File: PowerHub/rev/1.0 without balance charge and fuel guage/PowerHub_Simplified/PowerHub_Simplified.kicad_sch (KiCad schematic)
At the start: 28 parts, among them J1 HUB_CONN_1_W_VBUS, J2 HUB_CONN_2_W_VBUS, J3 HUB_CONN_3, J4 HUB_CONN_4, J5 BATTERY-, J6 BATTERY+, J7 Charger, Q1 BC817, SW1 SW_SPST, U1 TPS565208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

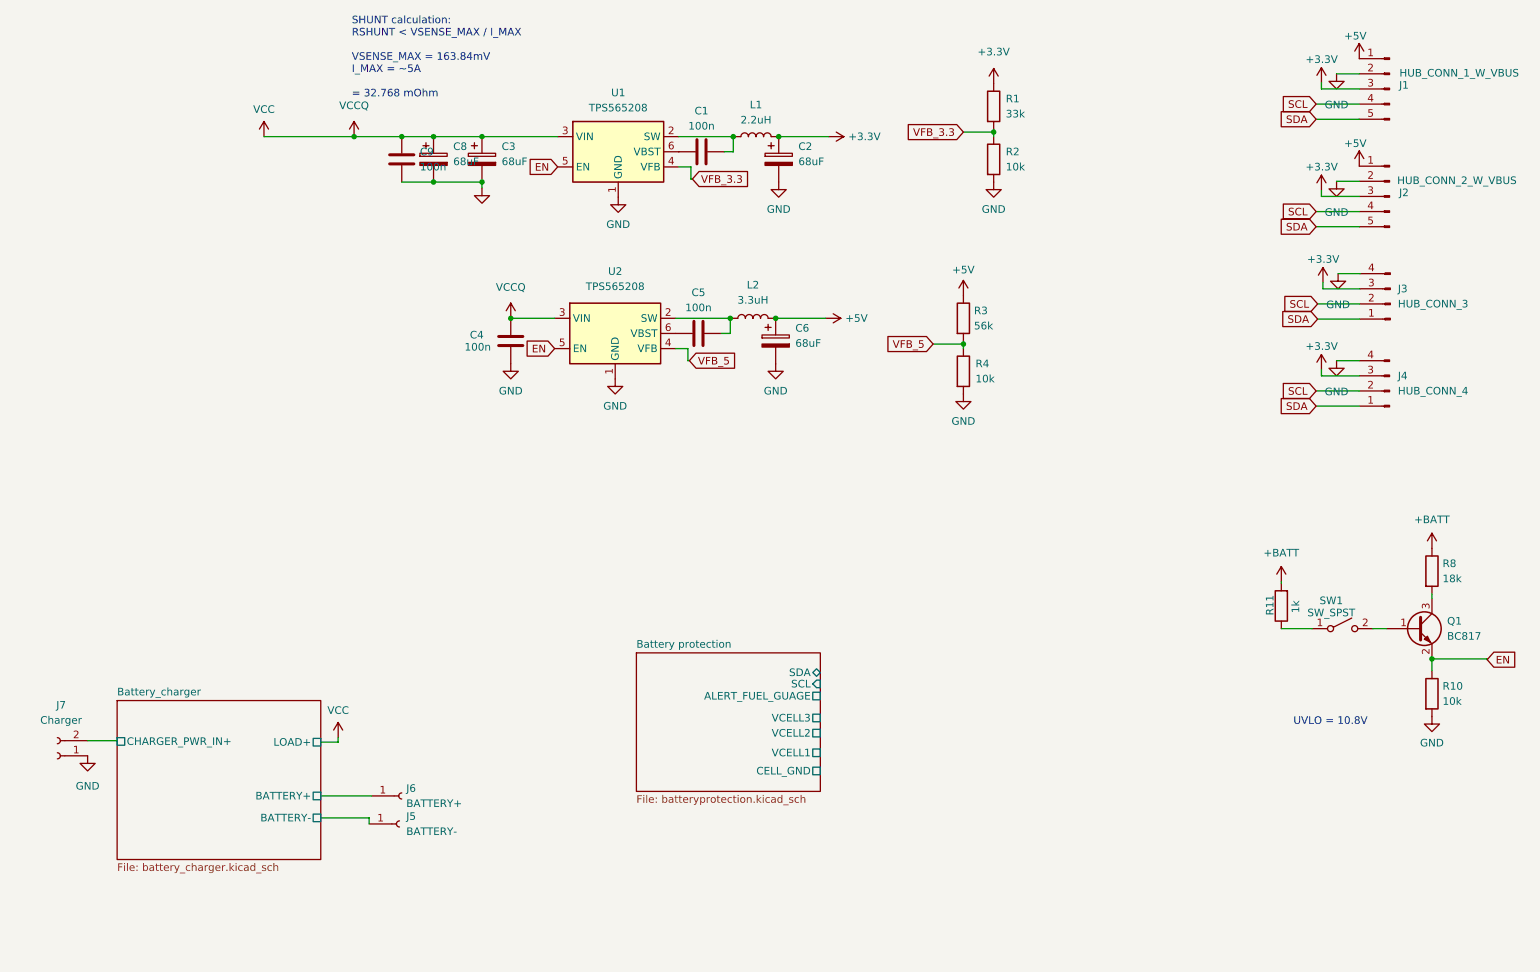
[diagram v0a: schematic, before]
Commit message: -add new version with charger circuit
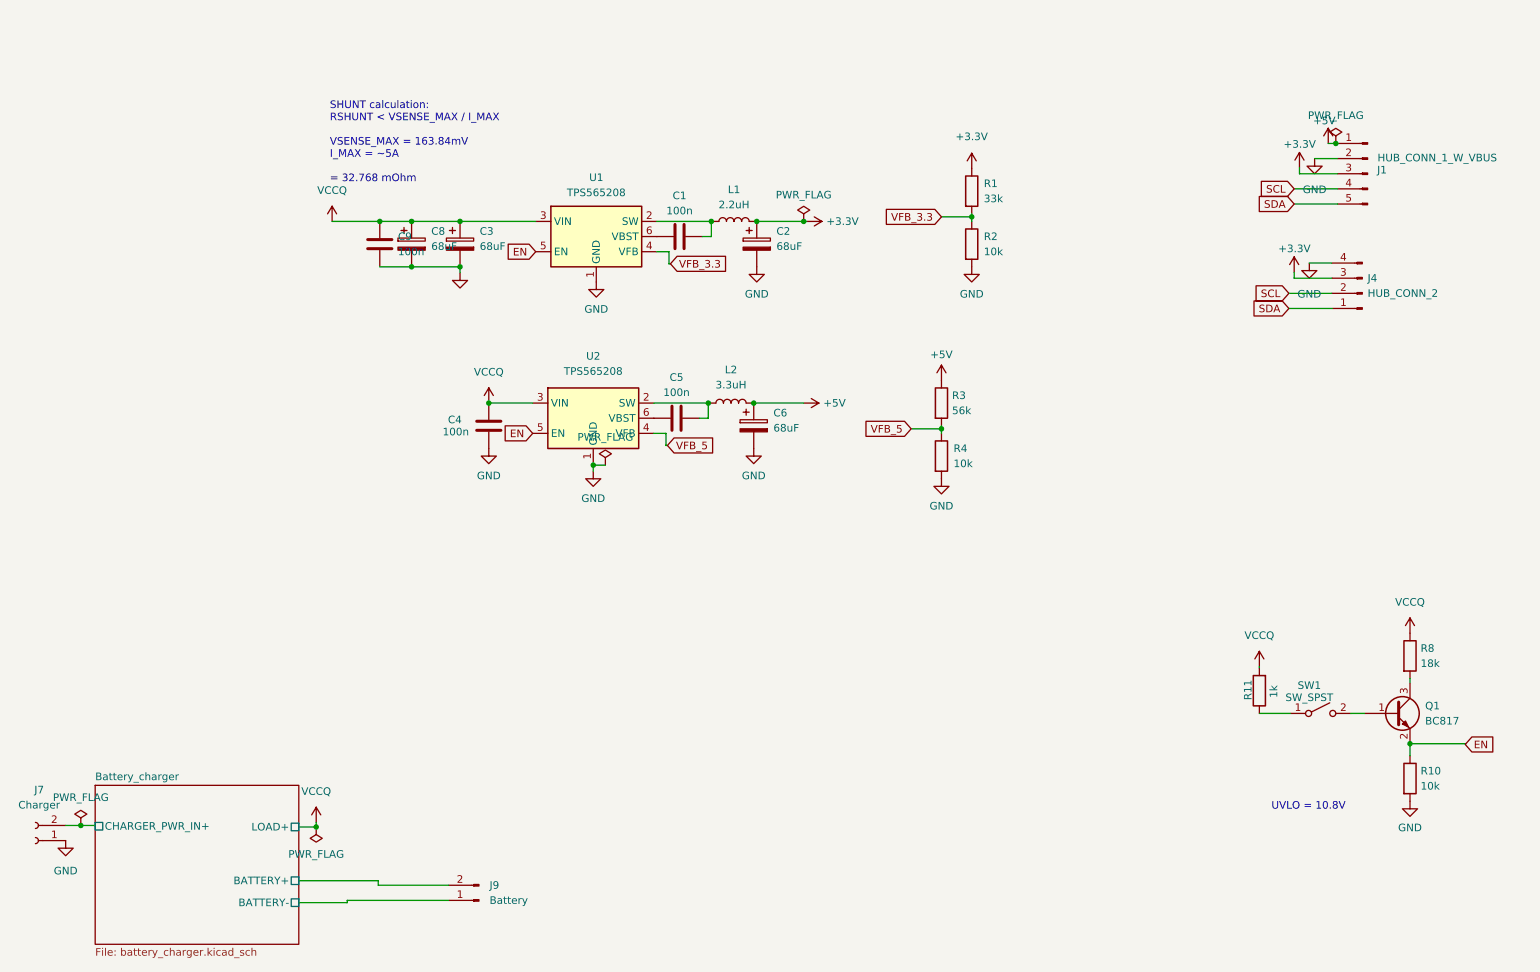
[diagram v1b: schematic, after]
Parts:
- removed J2: HUB_CONN_2_W_VBUS, symbol Connector:Conn_01x05_Pin
- removed J3: HUB_CONN_3, symbol Connector:Conn_01x04_Pin
- removed J5: BATTERY-, symbol Connector:Conn_01x01_Socket
- removed J6: BATTERY+, symbol Connector:Conn_01x01_Socket
- added J9: Battery, PowerHub_libs:1814773, symbol Connector:Conn_01x02_Pin
- C1, C4, C5, C9: footprint (none) -> Capacitor_SMD:C_0603_1608Metric_Pad1.08x0.95mm_HandSolder
- C2, C3, C6, C8: footprint (none) -> Capacitor_SMD:C_Elec_6.3x7.7
- J1: footprint (none) -> PowerHub_libs:1814809
- J4: value HUB_CONN_4 -> HUB_CONN_2; footprint (none) -> PowerHub_libs:SHDRRA4W60P0X250_1X4_1170X750X510P
- J7: footprint (none) -> PowerHub_libs:1814773
- L1, L2: footprint (none) -> Inductor_SMD:L_Abracon_ASPI-0630LR
- R1, R10, R11, R2, R3, R4, R8: footprint (none) -> Resistor_SMD:R_0603_1608Metric_Pad0.98x0.95mm_HandSolder
- SW1: footprint (none) -> Connector_PinHeader_2.54mm:PinHeader_1x02_P2.54mm_Vertical
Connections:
- net VCC is gone; now on net VCCQ: C3.1, C4.2, C8.1, C9.2, U1.3 (VIN), U2.3 (VIN)
- net Battery_charger/BATTERY+: now also J9.2 (Pin_2)
- net Battery_charger/BATTERY-: now also J9.1 (Pin_1)
- net +BATT renamed VCCQ
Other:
- removed sheet Battery protection
